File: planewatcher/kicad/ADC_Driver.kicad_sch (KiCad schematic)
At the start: 18 parts, among them U10 AD8138ARZ

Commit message: Add persistent PCBWay BOM fields to KiCad schematic
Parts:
- C46, C48, C73: MPN (none) -> GRM155R71H104KE14D; Manufacturer (none) -> Murata; Package (none) -> 0402
- C47: MPN (none) -> GRM188R61C106MA73D; Manufacturer (none) -> Murata; Package (none) -> 0603
- R28, R29: MPN (none) -> RC0402FR-0710KL; Manufacturer (none) -> Yageo; Package (none) -> 0402
- R30, R31: MPN (none) -> ERA-2AEB49R9X; Manufacturer (none) -> Panasonic; Package (none) -> 0402
- R37, R38, R39, R40: MPN (none) -> ERA-2AEB4990X; Manufacturer (none) -> Panasonic; Package (none) -> 0402
- U10: MPN (none) -> AD8138ARZ; Manufacturer (none) -> Analog Devices; Package (none) -> SOIC-8

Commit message: move power supply and add GPS module
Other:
- title: Plane Watcher: ADC Driver Section -> Plane Watcher
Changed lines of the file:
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@@
 	(paper "A4")
 	(title_block
-		(title "Plane Watcher: ADC Driver Section")
-		(date "2026-05-16")
-		(rev "prototype 1.1")
+		(title "Plane Watcher")
+		(date "2026-05-18")
+		(rev "prototype 1.2")
 		(company "plane.watch")
 	)

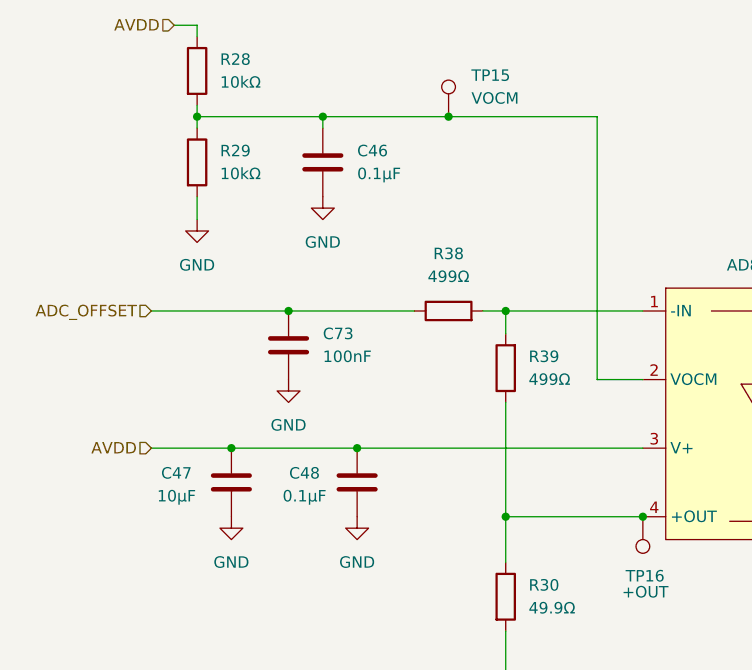
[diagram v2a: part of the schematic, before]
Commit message: review & consolidate all capacitors
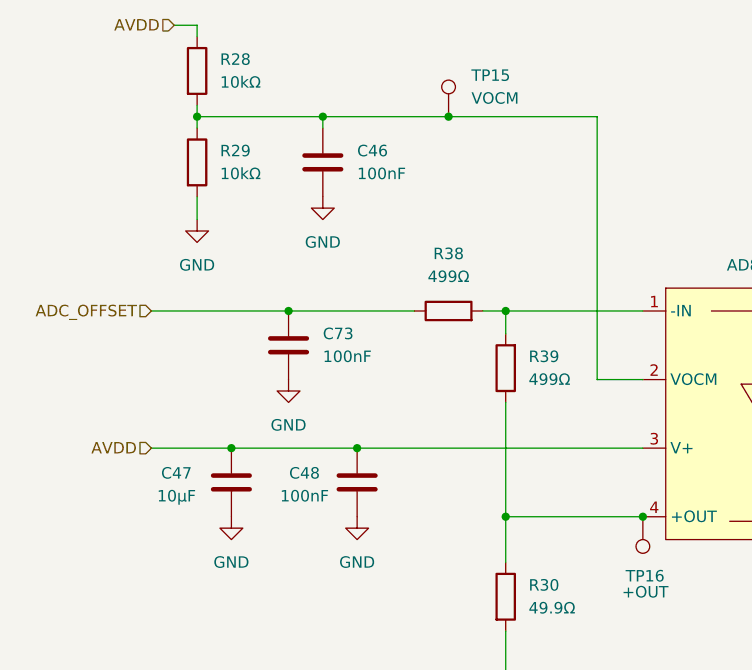
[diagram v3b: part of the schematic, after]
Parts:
- C46, C48: value 0.1µF -> 100nF; MPN GRM155R71H104KE14D -> GCM155R71A104KA55D; Manufacturer Murata -> Murata Electronics; Package 0402 -> 0402 (1005 Metric); Suggested Part Murata GRM155R71H104KE14D -> (none)
- C47: MPN GRM188R61C106MA73D -> GRM188Z71A106MA73J; Manufacturer Murata -> Murata Electronics; Package 0603 -> 0603 (1608 Metric); Suggested Part Murata GRM188R61C106MA73D -> (none)
- C71, C72: MPN (none) -> GJM1555C1H200FB01D; Manufacturer (none) -> Murata Electronics; Notes (none) -> Tuning capacitor footprint, C0G/NP0 0402 when fitted, DNP b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; Package (none) -> 0402 (1005 Metric); Suggested Part DNP by default; fit RF-grade C0G 0402 value selected during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 -> (none)
- C73: MPN GRM155R71H104KE14D -> GCM155R71A104KA55D; Manufacturer Murata -> Murata Electronics; Package 0402 -> 0402 (1005 Metric); Suggested Part Murata GRM155R71H104KE14D -> (none)
- R28, R29: Suggested Part Yageo RC0402FR-0710KL -> (none)
- R30, R31: Suggested Part Panasonic ERA-2AEB49R9X -> (none)
- R37, R38, R39, R40: Suggested Part Panasonic ERA-2AEB4990X -> (none)
- TP15, TP16, TP17: Suggested Part No fitted part (PCB pad only) -> (none)
- U10: Suggested Part Analog Devices AD8138ARZ -> (none)

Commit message: review & consolidate all resistors
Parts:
- R28, R29: MPN RC0402FR-0710KL -> RE0402BRE0710KL; Manufacturer Yageo -> YAGEO; Package 0402 -> 0402 (1005 Metric)
- R30, R31: MPN ERA-2AEB49R9X -> ERA-2VEB49R9X; Manufacturer Panasonic -> Panasonic Industry; Package 0402 -> 0402 (1005 Metric)
- R37, R38, R39, R40: MPN ERA-2AEB4990X -> RG1005N-4990-W-T1; Manufacturer Panasonic -> Susumu; Package 0402 -> 0402 (1005 Metric)
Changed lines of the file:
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@@
 			)
 		)
-		(property "Datasheet" ""
+		(property "Datasheet" "https://industrial.panasonic.com/cdbs/www-data/pdf/RDM0000/RDM0000C331.pdf"
 			(at 80.01 111.76 0)
 			(hide yes)
@@
 			)
 		)
-		(property "Description" "49.9Ω, ±0.1%, thin film, ≤25ppm/°C, 0402 chip resistor"
+		(property "Description" "49.9 Ohms ±0.1% 0.1W, 1/10W Chip Resistor 0402 (1005 Metric) Anti-Sulfur, Automotive AEC-Q200 Thin Film"
 			(at 80.01 111.76 0)
 			(hide yes)
@@
 			)
 		)
-		(property "Package" "0402"
+		(property "Package" "0402 (1005 Metric)"
 			(at 80.01 111.76 0)
 			(hide yes)
@@
 			)
 		)
-		(property "MPN" "ERA-2AEB49R9X"
+		(property "MPN" "ERA-2VEB49R9X"
 			(at 80.01 111.76 0)
 			(hide yes)
@@
 			)
 		)
-		(property "Manufacturer" "Panasonic"
+		(property "Manufacturer" "Panasonic Industry"
 			(at 80.01 111.76 0)
 			(hide yes)
@@
 			)
 		)
-		(property "Datasheet" ""
+		(property "Datasheet" "https://www.susumu.co.jp/dl/?filename=n_catalog_partition01_en.pdf&type=application/pdf"
 			(at 80.01 86.36 0)
 			(hide yes)
@@
 			)
 		)
-		(property "Description" "499Ω, ±0.1%, thin film, ≤25ppm/°C, 0402 chip resistor"
+		(property "Description" "499 Ohms ±0.05% 0.063W, 1/16W Chip Resistor 0402 (1005 Metric) Anti-Sulfur, Automotive AEC-Q200 Thin Film"
 			(at 80.01 86.36 0)
 			(hide yes)
@@
 			)
 		)
-		(property "Package" "0402"
+		(property "Package" "0402 (1005 Metric) "
 			(at 80.01 86.36 0)
 			(hide yes)
@@
 			)
 		)
-		(property "MPN" "ERA-2AEB4990X"
+		(property "MPN" "RG1005N-4990-W-T1"
 			(at 80.01 86.36 0)
 			(hide yes)
@@
 			)
 		)
-		(property "Manufacturer" "Panasonic"
+		(property "Manufacturer" "Susumu"
 			(at 80.01 86.36 0)
 			(hide yes)
@@
 			)
 		)
-		(property "Datasheet" ""
+		(property "Datasheet" "https://industrial.panasonic.com/cdbs/www-data/pdf/RDM0000/RDM0000C331.pdf"
 			(at 139.7 111.76 0)
 			(hide yes)
@@
 			)
 		)
-		(property "Description" "49.9Ω, ±0.1%, thin film, ≤25ppm/°C, 0402 chip resistor"
+		(property "Description" "49.9 Ohms ±0.1% 0.1W, 1/10W Chip Resistor 0402 (1005 Metric) Anti-Sulfur, Automotive AEC-Q200 Thin Film"
 			(at 139.7 111.76 0)
 			(hide yes)
@@
 			)
 		)
-		(property "Package" "0402"
+		(property "Package" "0402 (1005 Metric)"
 			(at 139.7 111.76 0)
 			(hide yes)
@@
 			)
 		)
-		(property "MPN" "ERA-2AEB49R9X"
+		(property "MPN" "ERA-2VEB49R9X"
 			(at 139.7 111.76 0)
 			(hide yes)
@@
 			)
 		)
-		(property "Manufacturer" "Panasonic"
+		(property "Manufacturer" "Panasonic Industry"
 			(at 139.7 111.76 0)
 			(hide yes)
@@
 			)
 		)
-		(property "Datasheet" ""
+		(property "Datasheet" "https://www.susumu.co.jp/dl/?filename=n_catalog_partition01_en.pdf&type=application/pdf"
 			(at 73.66 80.01 0)
 			(hide yes)
@@
 			)
 		)
-		(property "Description" "499Ω, ±0.1%, thin film, ≤25ppm/°C, 0402 chip resistor"
+		(property "Description" "499 Ohms ±0.05% 0.063W, 1/16W Chip Resistor 0402 (1005 Metric) Anti-Sulfur, Automotive AEC-Q200 Thin Film"
 			(at 73.66 80.01 0)
 			(hide yes)
@@
 			)
 		)
-		(property "Package" "0402"
+		(property "Package" "0402 (1005 Metric) "
 			(at 73.66 80.01 0)
 			(hide yes)
@@
 			)
 		)
-		(property "MPN" "ERA-2AEB4990X"
+		(property "MPN" "RG1005N-4990-W-T1"
 			(at 73.66 80.01 0)
 			(hide yes)
@@
 			)
 		)
-		(property "Manufacturer" "Panasonic"
+		(property "Manufacturer" "Susumu"
 			(at 73.66 80.01 0)
 			(hide yes)
@@
 			)
 		)
-		(property "Datasheet" ""
+		(property "Datasheet" "https://www.susumu.co.jp/dl/?filename=n_catalog_partition01_en.pdf&type=application/pdf"
 			(at 146.05 80.01 0)
 			(hide yes)
@@
 			)
 		)
-		(property "Description" "499Ω, ±0.1%, thin film, ≤25ppm/°C, 0402 chip resistor"
+		(property "Description" "499 Ohms ±0.05% 0.063W, 1/16W Chip Resistor 0402 (1005 Metric) Anti-Sulfur, Automotive AEC-Q200 Thin Film"
 			(at 146.05 80.01 0)
 			(hide yes)
@@
 			)
 		)
-		(property "Package" "0402"
+		(property "Package" "0402 (1005 Metric) "
 			(at 146.05 80.01 0)
 			(hide yes)
@@
 			)
 		)
-		(property "MPN" "ERA-2AEB4990X"
+		(property "MPN" "RG1005N-4990-W-T1"
 			(at 146.05 80.01 0)
 			(hide yes)
@@
 			)
 		)
-		(property "Manufacturer" "Panasonic"
+		(property "Manufacturer" "Susumu"
 			(at 146.05 80.01 0)
 			(hide yes)
@@
 			)
 		)
-		(property "Datasheet" ""
+		(property "Datasheet" "https://yageogroup.com/content/Resource%20Library/Datasheet/PYU-RE_105_ROHS_L.pdf"
 			(at 45.72 63.5 0)
 			(hide yes)
@@
 			)
 		)
-		(property "Description" "10kΩ, ±1%, thick film, 100ppm/°C, 0402 chip resistor"
+		(property "Description" "10 kOhms ±0.1% 0.063W, 1/16W Chip Resistor 0402 (1005 Metric) Thick Film"
 			(at 45.72 63.5 0)
 			(hide yes)
@@
 			)
 		)
-		(property "Package" "0402"
+		(property "Package" "0402 (1005 Metric)"
 			(at 45.72 63.5 0)
 			(hide yes)
@@
 			)
 		)
-		(property "MPN" "RC0402FR-0710KL"
+		(property "MPN" "RE0402BRE0710KL"
 			(at 45.72 63.5 0)
 			(hide yes)
@@
 			)
 		)
-		(property "Manufacturer" "Yageo"
+		(property "Manufacturer" "YAGEO"
 			(at 45.72 63.5 0)
 			(hide yes)
@@
 			)
 		)
-		(property "Datasheet" ""
+		(property "Datasheet" "https://www.susumu.co.jp/dl/?filename=n_catalog_partition01_en.pdf&type=application/pdf"
 			(at 139.7 86.36 0)
 			(hide yes)
@@
 			)
 		)
-		(property "Description" "499Ω, ±0.1%, thin film, ≤25ppm/°C, 0402 chip resistor"
+		(property "Description" "499 Ohms ±0.05% 0.063W, 1/16W Chip Resistor 0402 (1005 Metric) Anti-Sulfur, Automotive AEC-Q200 Thin Film"
 			(at 139.7 86.36 0)
 			(hide yes)
@@
 			)
 		)
-		(property "Package" "0402"
+		(property "Package" "0402 (1005 Metric) "
 			(at 139.7 86.36 0)
 			(hide yes)
@@
 			)
 		)
-		(property "MPN" "ERA-2AEB4990X"
+		(property "MPN" "RG1005N-4990-W-T1"
 			(at 139.7 86.36 0)
 			(hide yes)
@@
 			)
 		)
-		(property "Manufacturer" "Panasonic"
+		(property "Manufacturer" "Susumu"
 			(at 139.7 86.36 0)
 			(hide yes)
@@
 			)
 		)
-		(property "Datasheet" ""
+		(property "Datasheet" "https://yageogroup.com/content/Resource%20Library/Datasheet/PYU-RE_105_ROHS_L.pdf"
 			(at 45.72 53.34 0)
 			(hide yes)
@@
 			)
 		)
-		(property "Description" "10kΩ, ±1%, thick film, 100ppm/°C, 0402 chip resistor"
+		(property "Description" "10 kOhms ±0.1% 0.063W, 1/16W Chip Resistor 0402 (1005 Metric) Thick Film"
 			(at 45.72 53.34 0)
 			(hide yes)
@@
 			)
 		)
-		(property "Package" "0402"
+		(property "Package" "0402 (1005 Metric)"
 			(at 45.72 53.34 0)
 			(hide yes)
@@
 			)
 		)
-		(property "MPN" "RC0402FR-0710KL"
+		(property "MPN" "RE0402BRE0710KL"
 			(at 45.72 53.34 0)
 			(hide yes)
@@
 			)
 		)
-		(property "Manufacturer" "Yageo"
+		(property "Manufacturer" "YAGEO"
 			(at 45.72 53.34 0)
 			(hide yes)

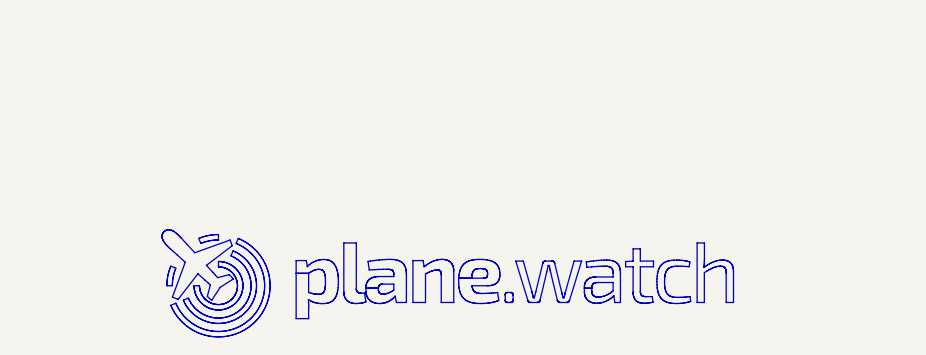
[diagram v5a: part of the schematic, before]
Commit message: add license & copyright info to schematic and pcb. fix layer window.
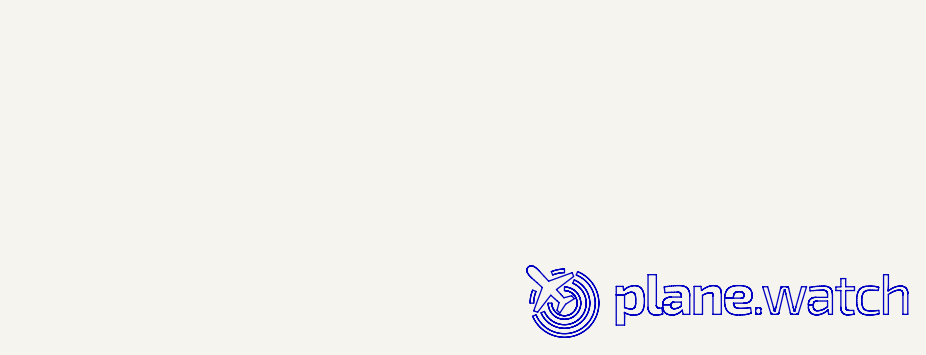
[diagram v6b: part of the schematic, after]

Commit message: added lcsc_ids to all parts
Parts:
- C46, C48, C73: lcsc_id (none) -> C161163
- C47: MPN GRM188Z71A106MA73J -> GRM188Z71A106MA73D; lcsc_id (none) -> C237435
- C71, C72: lcsc_id (none) -> C913479
- R28, R29: lcsc_id (none) -> C4140200
- R30, R31: lcsc_id (none) -> C4103766
- R37, R38, R39, R40: lcsc_id (none) -> C4184281
- U10: lcsc_id (none) -> C113762
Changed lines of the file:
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@@
+			)
+		)
+		(property "lcsc_id" "C4103766"
+			(at 80.01 111.76 0)
+			(hide yes)
+			(show_name no)
+			(do_not_autoplace no)
+			(effects
+				(font
+					(size 1.27 1.27)
+				)
 			)
 		)
@@
 			)
 		)
+		(property "lcsc_id" "C161163"
+			(at 55.88 83.82 0)
+			(hide yes)
+			(show_name no)
+			(do_not_autoplace no)
+			(effects
+				(font
+					(size 1.27 1.27)
+				)
+			)
+		)
 		(pin "1"
 		)
@@
 			)
 		)
+		(property "lcsc_id" "C4184281"
+			(at 80.01 86.36 0)
+			(hide yes)
+			(show_name no)
+			(do_not_autoplace no)
+			(effects
+				(font
+					(size 1.27 1.27)
+				)
+			)
+		)
 		(pin "2"
 		)
@@
 			)
 		)
+		(property "lcsc_id" "C4103766"
+			(at 139.7 111.76 0)
+			(hide yes)
+			(show_name no)
+			(do_not_autoplace no)
+			(effects
+				(font
+					(size 1.27 1.27)
+				)
+			)
+		)
 		(pin "2"
 		)
@@
 			)
 		)
+		(property "lcsc_id" "C4184281"
+			(at 73.66 80.01 0)
+			(hide yes)
+			(show_name no)
+			(do_not_autoplace no)
+			(effects
+				(font
+					(size 1.27 1.27)
+				)
+			)
+		)
 		(pin "2"
 		)
@@
 			)
 		)
+		(property "lcsc_id" "C161163"
+			(at 59.69 63.5 0)
+			(hide yes)
+			(show_name no)
+			(do_not_autoplace no)
+			(effects
+				(font
+					(size 1.27 1.27)
+				)
+			)
+		)
 		(pin "2"
 		)
@@
 			)
 		)
+		(property "lcsc_id" "C4184281"
+			(at 146.05 80.01 0)
+			(hide yes)
+			(show_name no)
+			(do_not_autoplace no)
+			(effects
+				(font
+					(size 1.27 1.27)
+				)
+			)
+		)
 		(pin "2"
 		)
@@
 			)
 		)
+		(property "lcsc_id" "C113762"
+			(at 109.22 74.93 0)
+			(hide yes)
+			(show_name no)
+			(do_not_autoplace no)
+			(effects
+				(font
+					(size 1.27 1.27)
+				)
+			)
+		)
 		(pin "7"
 		)
@@
 			)
 		)
+		(property "lcsc_id" "C913479"
+			(at 134.62 130.81 90)
+			(hide yes)
+			(show_name no)
+			(do_not_autoplace no)
+			(effects
+				(font
+					(size 1.27 1.27)
+				)
+			)
+		)
 		(pin "1"
 		)
@@
 			)
 		)
+		(property "lcsc_id" "C4140200"
+			(at 45.72 63.5 0)
+			(hide yes)
+			(show_name no)
+			(do_not_autoplace no)
+			(effects
+				(font
+					(size 1.27 1.27)
+				)
+			)
+		)
 		(pin "1"
 		)
@@
 			)
 		)
+		(property "lcsc_id" "C161163"
+			(at 63.5 99.06 0)
+			(hide yes)
+			(show_name no)
+			(do_not_autoplace no)
+			(effects
+				(font
+					(size 1.27 1.27)
+				)
+			)
+		)
 		(pin "1"
 		)
@@
 			)
 		)
-		(property "MPN" "GRM188Z71A106MA73J"
+		(property "MPN" "GRM188Z71A106MA73D"
 			(at 49.53 99.06 0)
 			(hide yes)
@@
 		(property "Notes" ""
 			(at 49.53 99.06 90)
+			(hide yes)
+			(show_name no)
+			(do_not_autoplace no)
+			(effects
+				(font
+					(size 1.27 1.27)
+				)
+			)
+		)
+		(property "lcsc_id" "C237435"
+			(at 49.53 99.06 0)
 			(hide yes)
 			(show_name no)
@@
 			)
 		)
+		(property "lcsc_id" "C4184281"
+			(at 139.7 86.36 0)
+			(hide yes)
+			(show_name no)
+			(do_not_autoplace no)
+			(effects
+				(font
+					(size 1.27 1.27)
+				)
+			)
+		)
 		(pin "2"
 		)
@@
 			)
 		)
+		(property "lcsc_id" "C913479"
+			(at 85.09 130.81 90)
+			(hide yes)
+			(show_name no)
+			(do_not_autoplace no)
+			(effects
+				(font
+					(size 1.27 1.27)
+				)
+			)
+		)
 		(pin "1"
 		)
@@
 			(at 45.72 53.34 0)
 			(hide yes)
+			(show_name no)
+			(do_not_autoplace no)
+			(effects
+				(font
+					(size 1.27 1.27)
+				)
+			)
+		)
+		(property "lcsc_id" "C4140200"
+			(at 45.72 53.34 0)
+			(hide yes)

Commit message: update BoM to available parts from LCSC
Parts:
- R28, R29: MPN RE0402BRE0710KL -> ERA-2AEB103X; Manufacturer YAGEO -> Panasonic Industry; lcsc_id C4140200 -> C191915
- R30, R31: MPN ERA-2VEB49R9X -> RT0402BRD0749R9L; Manufacturer Panasonic Industry -> YAGEO; lcsc_id C4103766 -> C852809
- R37, R38, R39, R40: MPN RG1005N-4990-W-T1 -> RN73C1E499RBTD; Manufacturer Susumu -> TE Connectivity; lcsc_id C4184281 -> C2090004
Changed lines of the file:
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@@
 			)
 		)
-		(property "Description" "49.9 Ohms ±0.1% 0.1W, 1/10W Chip Resistor 0402 (1005 Metric) Anti-Sulfur, Automotive AEC-Q200 Thin Film"
+		(property "Description" "49.9Ω 63mW 50V Thin Film Resistor ±25ppm/℃ ±0.1% 0402 Chip Resistor - Surface Mount RoHS"
 			(at 80.01 111.76 0)
 			(hide yes)
@@
 			)
 		)
-		(property "MPN" "ERA-2VEB49R9X"
+		(property "MPN" "RT0402BRD0749R9L"
 			(at 80.01 111.76 0)
 			(hide yes)
@@
 			)
 		)
-		(property "Manufacturer" "Panasonic Industry"
+		(property "Manufacturer" "YAGEO"
 			(at 80.01 111.76 0)
 			(hide yes)
@@
 			)
 		)
-		(property "lcsc_id" "C4103766"
+		(property "lcsc_id" "C852809"
 			(at 80.01 111.76 0)
 			(hide yes)
@@
 			)
 		)
-		(property "Description" "499 Ohms ±0.05% 0.063W, 1/16W Chip Resistor 0402 (1005 Metric) Anti-Sulfur, Automotive AEC-Q200 Thin Film"
+		(property "Description" "63mW 499Ω 25V Thin Film Resistor ±0.1% ±10ppm/℃ 0402 Chip Resistor - Surface Mount RoHS"
 			(at 80.01 86.36 0)
 			(hide yes)
@@
 			)
 		)
-		(property "MPN" "RG1005N-4990-W-T1"
+		(property "MPN" "RN73C1E499RBTD"
 			(at 80.01 86.36 0)
 			(hide yes)
@@
 			)
 		)
-		(property "Manufacturer" "Susumu"
+		(property "Manufacturer" "TE Connectivity"
 			(at 80.01 86.36 0)
 			(hide yes)
@@
 			)
 		)
-		(property "lcsc_id" "C4184281"
+		(property "lcsc_id" "C2090004"
 			(at 80.01 86.36 0)
 			(hide yes)
@@
 			)
 		)
-		(property "Description" "49.9 Ohms ±0.1% 0.1W, 1/10W Chip Resistor 0402 (1005 Metric) Anti-Sulfur, Automotive AEC-Q200 Thin Film"
+		(property "Description" "49.9Ω 63mW 50V Thin Film Resistor ±25ppm/℃ ±0.1% 0402 Chip Resistor - Surface Mount RoHS"
 			(at 139.7 111.76 0)
 			(hide yes)
@@
 			)
 		)
-		(property "MPN" "ERA-2VEB49R9X"
+		(property "MPN" "RT0402BRD0749R9L"
 			(at 139.7 111.76 0)
 			(hide yes)
@@
 			)
 		)
-		(property "Manufacturer" "Panasonic Industry"
+		(property "Manufacturer" "YAGEO"
 			(at 139.7 111.76 0)
 			(hide yes)
@@
 			)
 		)
-		(property "lcsc_id" "C4103766"
+		(property "lcsc_id" "C852809"
 			(at 139.7 111.76 0)
 			(hide yes)
@@
 			)
 		)
-		(property "Description" "499 Ohms ±0.05% 0.063W, 1/16W Chip Resistor 0402 (1005 Metric) Anti-Sulfur, Automotive AEC-Q200 Thin Film"
+		(property "Description" "63mW 499Ω 25V Thin Film Resistor ±0.1% ±10ppm/℃ 0402 Chip Resistor - Surface Mount RoHS"
 			(at 73.66 80.01 0)
 			(hide yes)
@@
 			)
 		)
-		(property "MPN" "RG1005N-4990-W-T1"
+		(property "MPN" "RN73C1E499RBTD"
 			(at 73.66 80.01 0)
 			(hide yes)
@@
 			)
 		)
-		(property "Manufacturer" "Susumu"
+		(property "Manufacturer" "TE Connectivity"
 			(at 73.66 80.01 0)
 			(hide yes)
@@
 			)
 		)
-		(property "lcsc_id" "C4184281"
+		(property "lcsc_id" "C2090004"
 			(at 73.66 80.01 0)
 			(hide yes)
@@
 			)
 		)
-		(property "Description" "499 Ohms ±0.05% 0.063W, 1/16W Chip Resistor 0402 (1005 Metric) Anti-Sulfur, Automotive AEC-Q200 Thin Film"
+		(property "Description" "63mW 499Ω 25V Thin Film Resistor ±0.1% ±10ppm/℃ 0402 Chip Resistor - Surface Mount RoHS"
 			(at 146.05 80.01 0)
 			(hide yes)
@@
 			)
 		)
-		(property "MPN" "RG1005N-4990-W-T1"
+		(property "MPN" "RN73C1E499RBTD"
 			(at 146.05 80.01 0)
 			(hide yes)
@@
 			)
 		)
-		(property "Manufacturer" "Susumu"
+		(property "Manufacturer" "TE Connectivity"
 			(at 146.05 80.01 0)
 			(hide yes)
@@
 			)
 		)
-		(property "lcsc_id" "C4184281"
+		(property "lcsc_id" "C2090004"
 			(at 146.05 80.01 0)
 			(hide yes)
@@
 			)
 		)
-		(property "Description" "10 kOhms ±0.1% 0.063W, 1/16W Chip Resistor 0402 (1005 Metric) Thick Film"
+		(property "Description" "10 kOhms ±0.1% 0.063W, 1/16W Chip Resistor 0402 (1005 Metric) Automotive AEC-Q200 Thin Film"
 			(at 45.72 63.5 0)
 			(hide yes)
@@
 			)
 		)
-		(property "MPN" "RE0402BRE0710KL"
+		(property "MPN" "ERA-2AEB103X"
 			(at 45.72 63.5 0)
 			(hide yes)
@@
 			)
 		)
-		(property "Manufacturer" "YAGEO"
+		(property "Manufacturer" "Panasonic Industry"
 			(at 45.72 63.5 0)
 			(hide yes)
@@
 			)
 		)
-		(property "lcsc_id" "C4140200"
+		(property "lcsc_id" "C191915"
 			(at 45.72 63.5 0)
 			(hide yes)
@@
 			)
 		)
-		(property "Description" "499 Ohms ±0.05% 0.063W, 1/16W Chip Resistor 0402 (1005 Metric) Anti-Sulfur, Automotive AEC-Q200 Thin Film"
+		(property "Description" "63mW 499Ω 25V Thin Film Resistor ±0.1% ±10ppm/℃ 0402 Chip Resistor - Surface Mount RoHS"
 			(at 139.7 86.36 0)
 			(hide yes)
@@
 			)
 		)
-		(property "MPN" "RG1005N-4990-W-T1"
+		(property "MPN" "RN73C1E499RBTD"
 			(at 139.7 86.36 0)
 			(hide yes)
@@
 			)
 		)
-		(property "Manufacturer" "Susumu"
+		(property "Manufacturer" "TE Connectivity"
 			(at 139.7 86.36 0)
 			(hide yes)
@@
 			)
 		)
-		(property "lcsc_id" "C4184281"
+		(property "lcsc_id" "C2090004"
 			(at 139.7 86.36 0)
 			(hide yes)
@@
 			)
 		)
-		(property "Description" "10 kOhms ±0.1% 0.063W, 1/16W Chip Resistor 0402 (1005 Metric) Thick Film"
+		(property "Description" "10 kOhms ±0.1% 0.063W, 1/16W Chip Resistor 0402 (1005 Metric) Automotive AEC-Q200 Thin Film"
 			(at 45.72 53.34 0)
 			(hide yes)
@@
 			)
 		)
-		(property "MPN" "RE0402BRE0710KL"
+		(property "MPN" "ERA-2AEB103X"
 			(at 45.72 53.34 0)
 			(hide yes)
@@
 			)
 		)
-		(property "Manufacturer" "YAGEO"
+		(property "Manufacturer" "Panasonic Industry"
 			(at 45.72 53.34 0)
 			(hide yes)
@@
 			)
 		)
-		(property "lcsc_id" "C4140200"
+		(property "lcsc_id" "C191915"
 			(at 45.72 53.34 0)
 			(hide yes)
